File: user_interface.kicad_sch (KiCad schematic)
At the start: 26 parts, among them J10 Line out, J11 Headphone, J2 SWD, J3 I2C, J4 GPIO_A, J5 GPIO_B, J6 SPI, J9 Serial

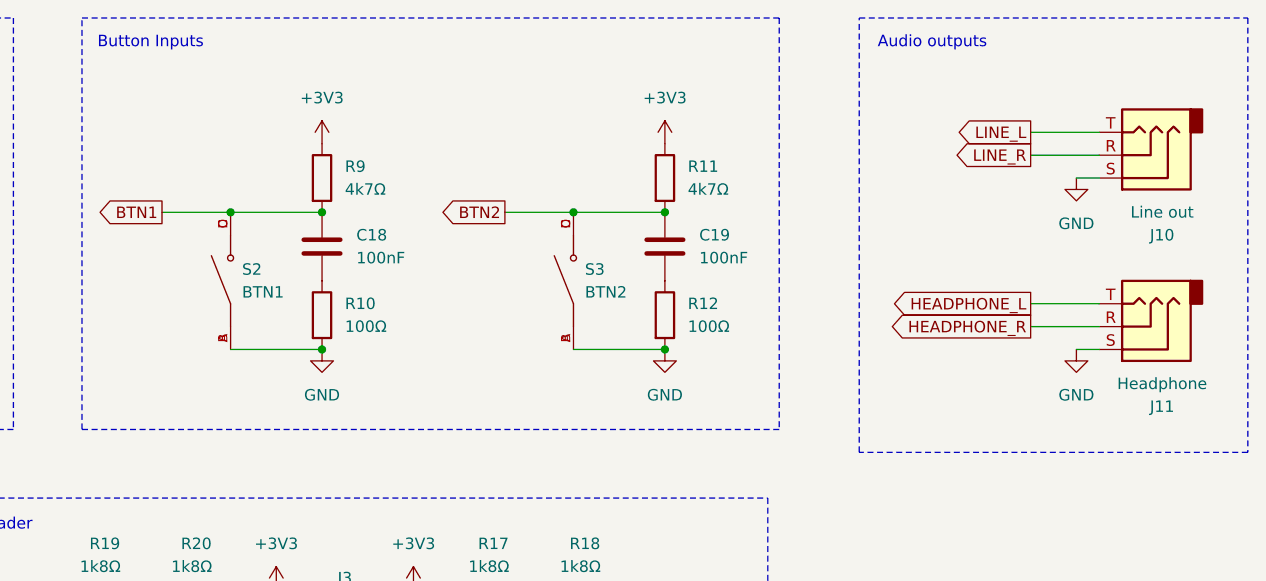
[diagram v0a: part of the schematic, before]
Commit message: Updated schematic with parts found in JLCPCB parts database. Updated footprints, 3d models for those items. All schematic symbols now have LCSC part numbers, footprints and 3D models. No PCB layout has been done.
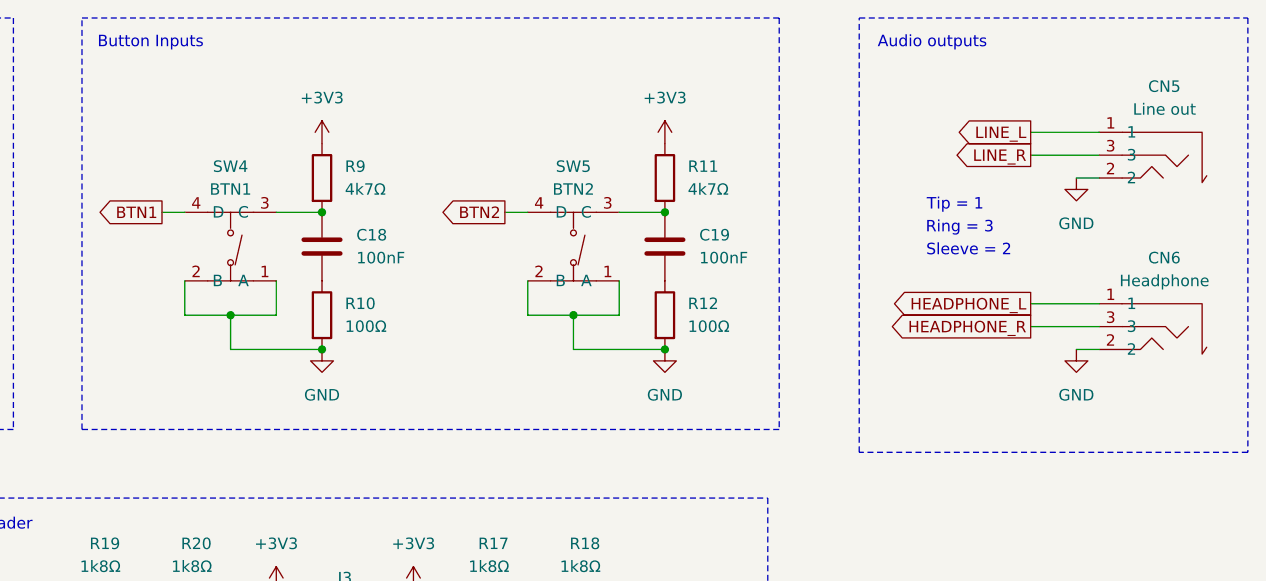
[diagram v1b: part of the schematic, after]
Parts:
- removed J10: Line out, symbol Connector_Audio:AudioJack3
- removed J11: Headphone, symbol Connector_Audio:AudioJack3
- removed S2: BTN1, stm-midi-poc1:SW_TS-1187A-B-A-B, symbol TS-1187A-B-A-B:TS-1187A-B-A-B
- removed S3: BTN2, stm-midi-poc1:SW_TS-1187A-B-A-B, symbol TS-1187A-B-A-B:TS-1187A-B-A-B
- added CN5: Line out, easyeda2kicad:AUDIO-SMD_PJ-321A-4A, symbol easyeda2kicad:PJ-321A-4A
- added CN6: Headphone, easyeda2kicad:AUDIO-SMD_PJ-321A-4A, symbol easyeda2kicad:PJ-321A-4A
- added SW4: BTN1, easyeda2kicad:SW-SMD_4P-L5.1-W5.1-P3.70-LS6.5-TL-2, symbol easyeda2kicad:TS-1187A-B-A-B
- added SW5: BTN2, easyeda2kicad:SW-SMD_4P-L5.1-W5.1-P3.70-LS6.5-TL-2, symbol easyeda2kicad:TS-1187A-B-A-B
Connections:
- net BTN1: now also SW4.4 (D); no longer C18.1, R9.2
- net BTN2: now also SW5.4 (D); no longer C19.1, R11.2
- net GND: now also CN5.2, CN6.2, SW4.1 (A), SW4.2 (B), SW5.1 (A), SW5.2 (B)
- net HEADPHONE_L: now also CN6.1
- net HEADPHONE_R: now also CN6.3
- net LINE_L: now also CN5.1
- net LINE_R: now also CN5.3
- new net: C18.1, R9.2, SW4.3 (C)
- new net: C19.1, R11.2, SW5.3 (C)
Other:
- note added: "Ring = 3"
- note added: "Sleeve = 2"
- note added: "Tip = 1"

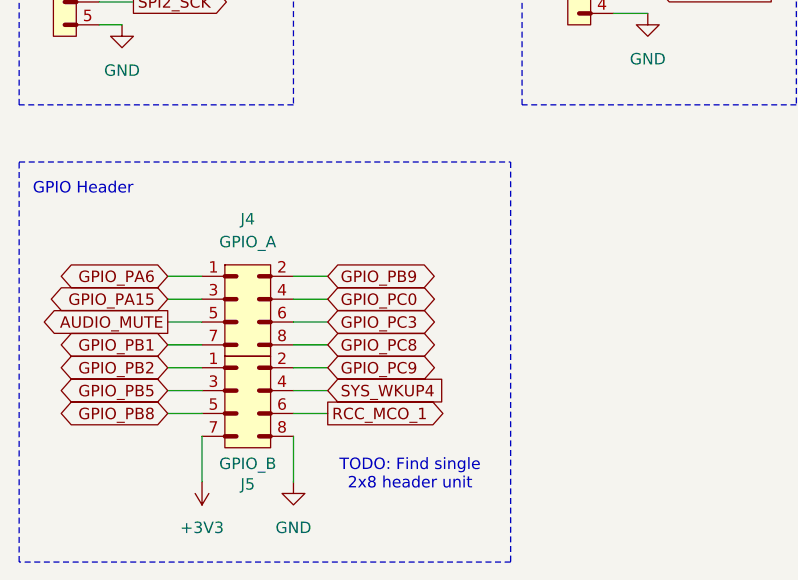
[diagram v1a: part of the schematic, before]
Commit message: Group PCB components together more. Replace 2x2x4 by 1x2x8 connector.
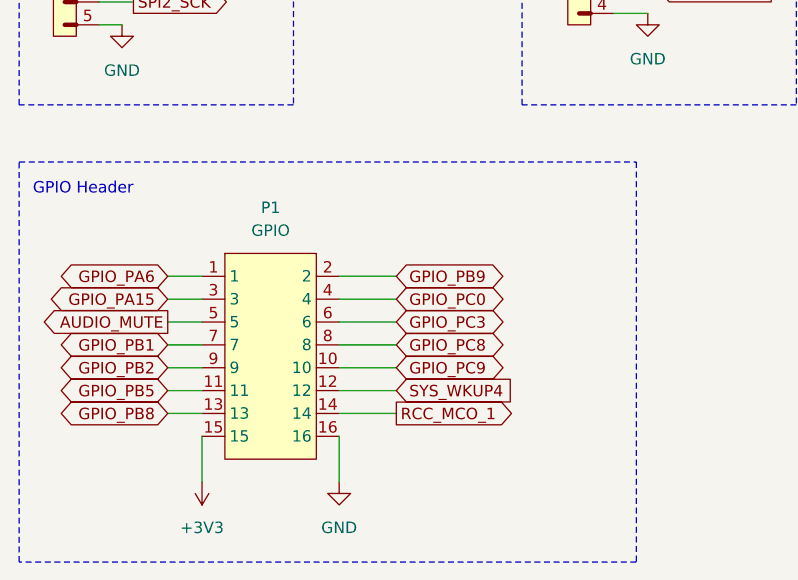
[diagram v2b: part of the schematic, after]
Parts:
- removed J4: GPIO_A, Connector_PinHeader_2.54mm:PinHeader_2x04_P2.54mm_Vertical, symbol PCM_SL_Pin_Headers:PINHD_2x4_Male
- removed J5: GPIO_B, Connector_PinHeader_2.54mm:PinHeader_2x04_P2.54mm_Vertical, symbol PCM_SL_Pin_Headers:PINHD_2x4_Male
- added P1: GPIO, easyeda2kicad:HDR-TH_16P-P2.54-V-M-R2-C8-S2.54, symbol easyeda2kicad:Header-Male-2.54_2x8
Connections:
- net +3V3: now also P1.15
- net AUDIO_MUTE: now also P1.5
- net GND: now also P1.16
- net GPIO_PA15: now also P1.3
- net GPIO_PA6: now also P1.1
- net GPIO_PB1: now also P1.7
- net GPIO_PB2: now also P1.9
- net GPIO_PB5: now also P1.11
- net GPIO_PB8: now also P1.13
- net GPIO_PB9: now also P1.2
- net GPIO_PC0: now also P1.4
- net GPIO_PC3: now also P1.6
- net GPIO_PC8: now also P1.8
- net GPIO_PC9: now also P1.10
- net RCC_MCO_1: now also P1.14
- net SYS_WKUP4: now also P1.12
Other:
- note removed: "TODO: Find single 2x8 header unit"

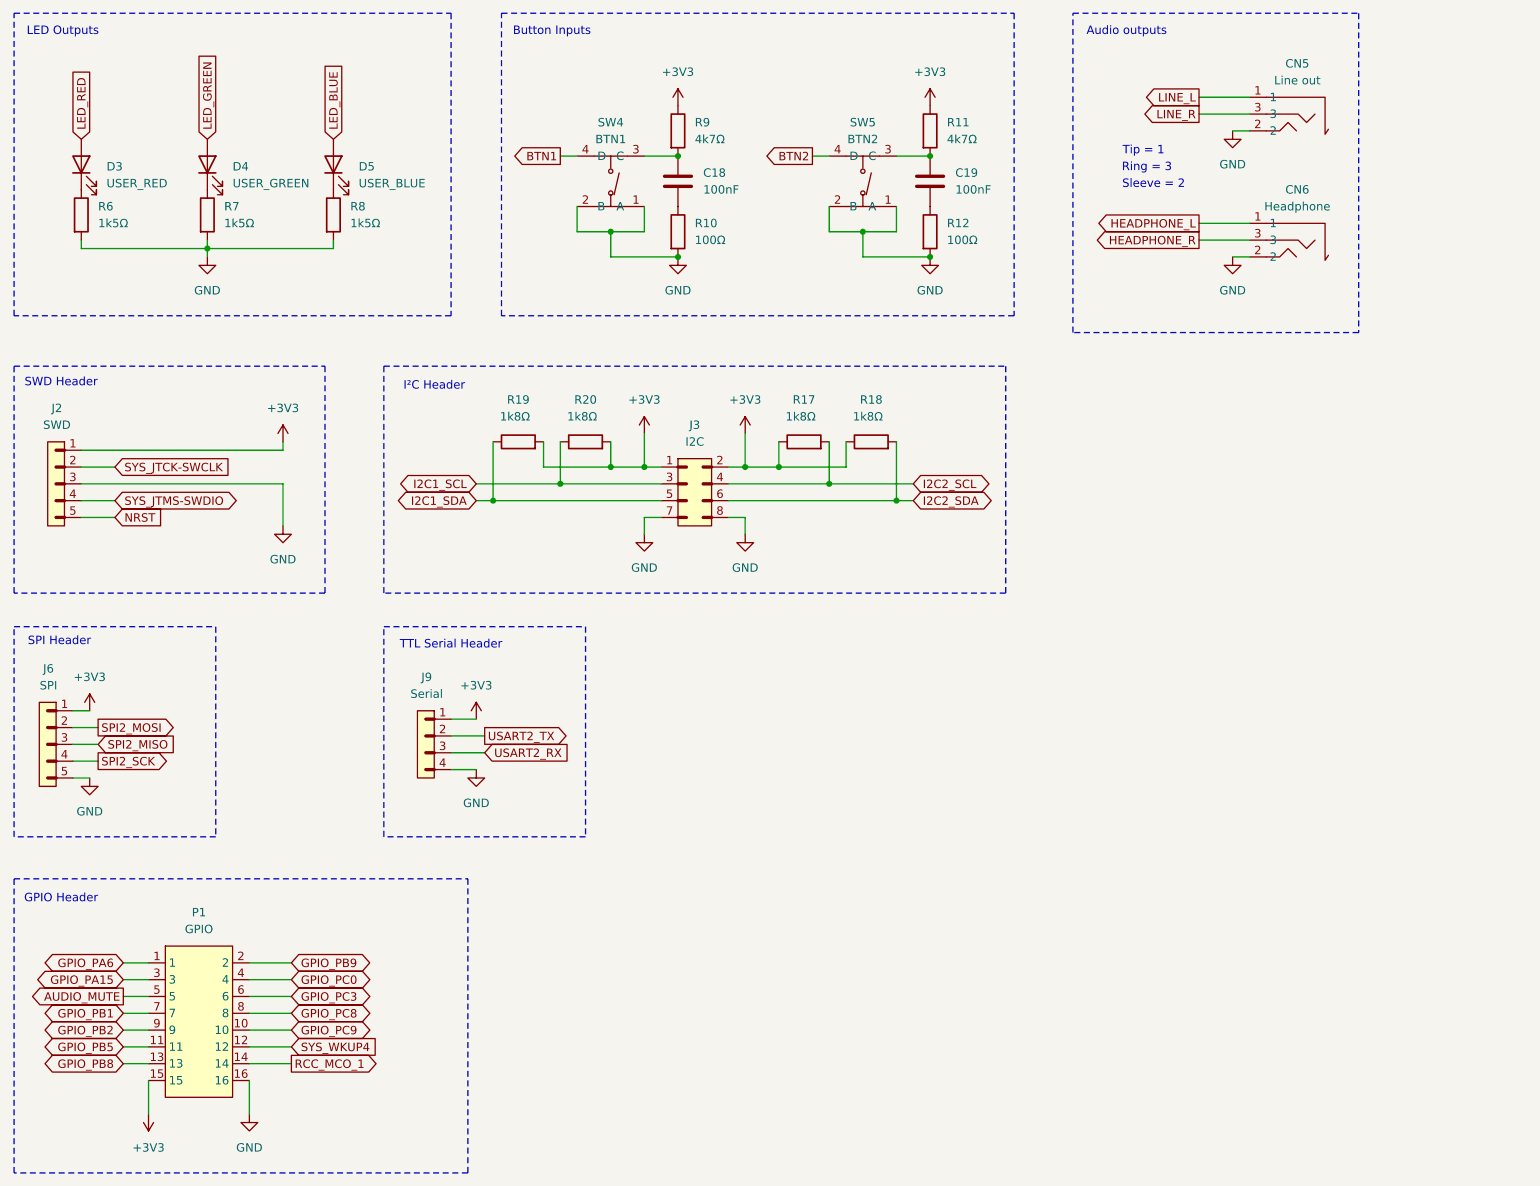
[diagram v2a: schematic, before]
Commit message: Create PCB outline and move components into better locations. (Not done yet!) Update schematic a little bit with additional nets and clarifications. Add mounting holes. Unify components/footprints.
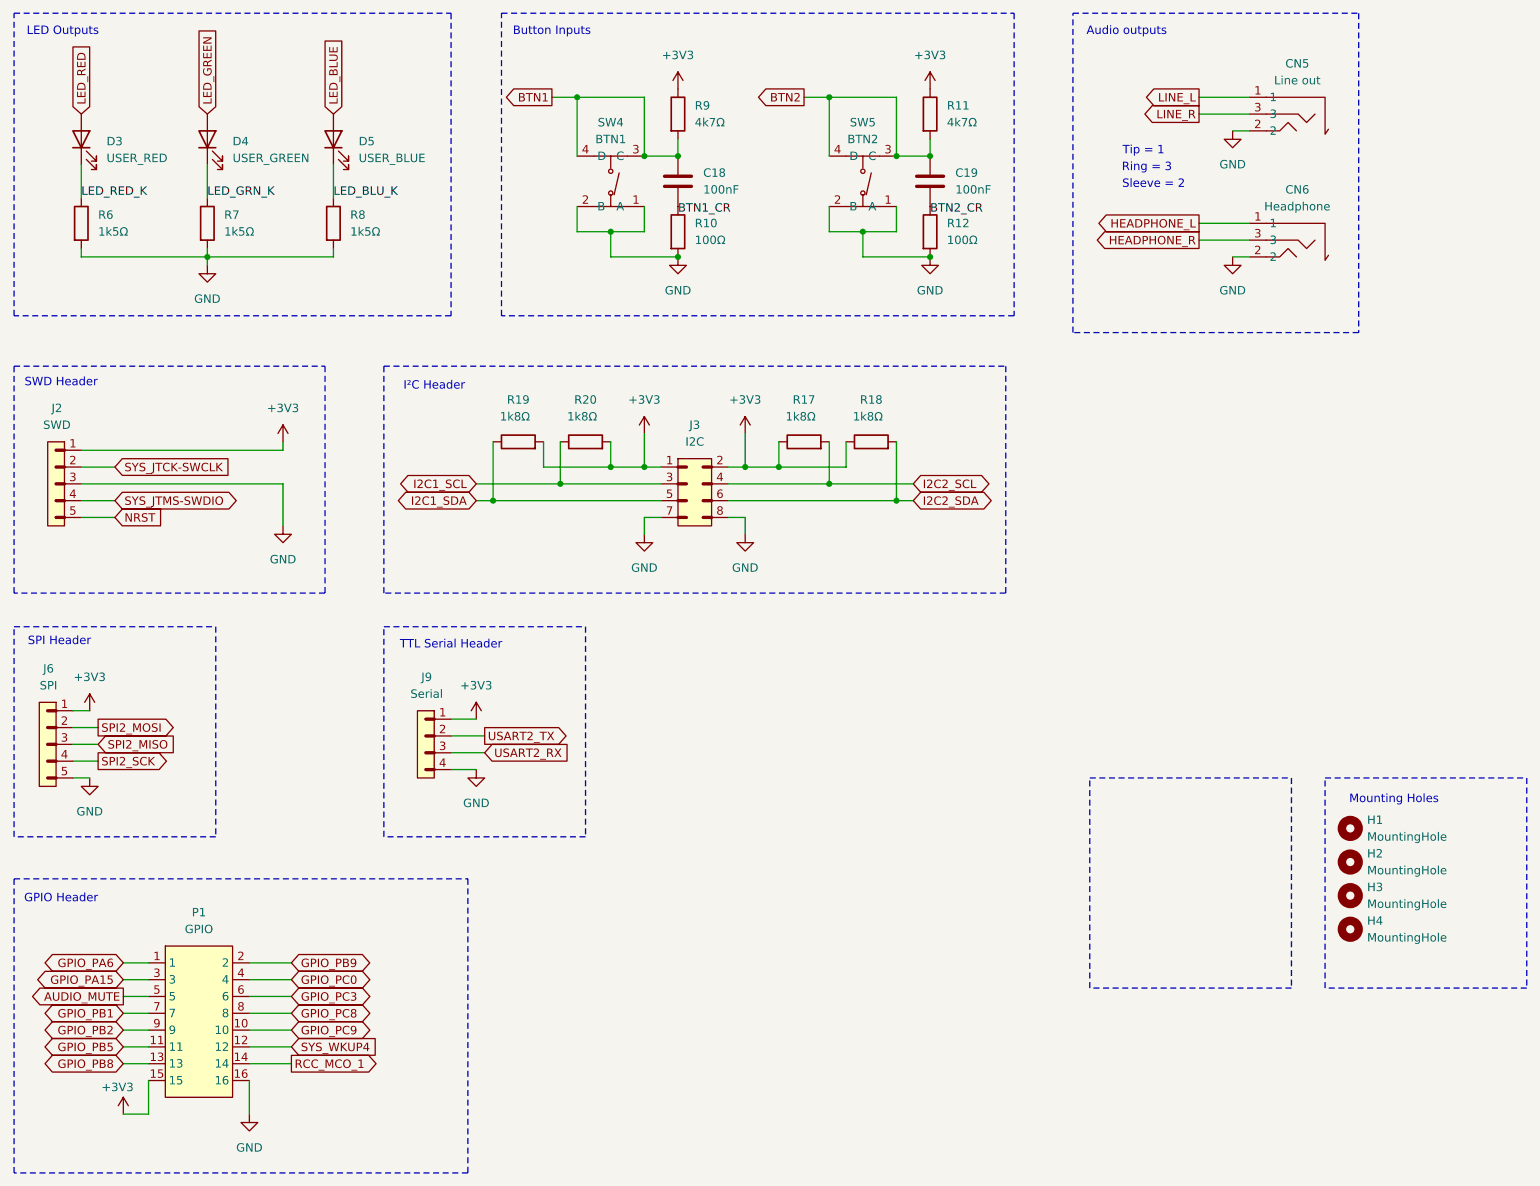
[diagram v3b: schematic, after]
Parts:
- added H1, H2, H3, H4: MountingHole, MountingHole:MountingHole_2.2mm_M2, symbol Mechanical:MountingHole
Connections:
- net BTN1: now also C18.1, R9.2, SW4.3 (C)
- net BTN2: now also C19.1, R11.2, SW5.3 (C)
- net LED_BLU_K: now reaches D5.1 (K), R8.1
- net LED_RED_K: now reaches D3.1 (K), R6.1
- net LED_GRN_K: now reaches D4.1 (K), R7.1
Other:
- note added: "Mounting Holes"
- moved on the sheet: D3, D4, D5, R11, R6, R7, R8, R9

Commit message: Work on power section and some miscellaneous small areas
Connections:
- net BTN1_CR: now also C18.2, R10.1
- net BTN2_CR: now also C19.2, R12.1
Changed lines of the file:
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@@
 	)
 	(label "BTN1_CR"
-		(at 133.35 49.53 0)
+		(at 133.35 48.26 0)
 		(fields_autoplaced yes)
 		(effects
@@
 	)
 	(label "BTN2_CR"
-		(at 171.45 49.53 0)
+		(at 171.45 48.26 0)
 		(fields_autoplaced yes)
 		(effects

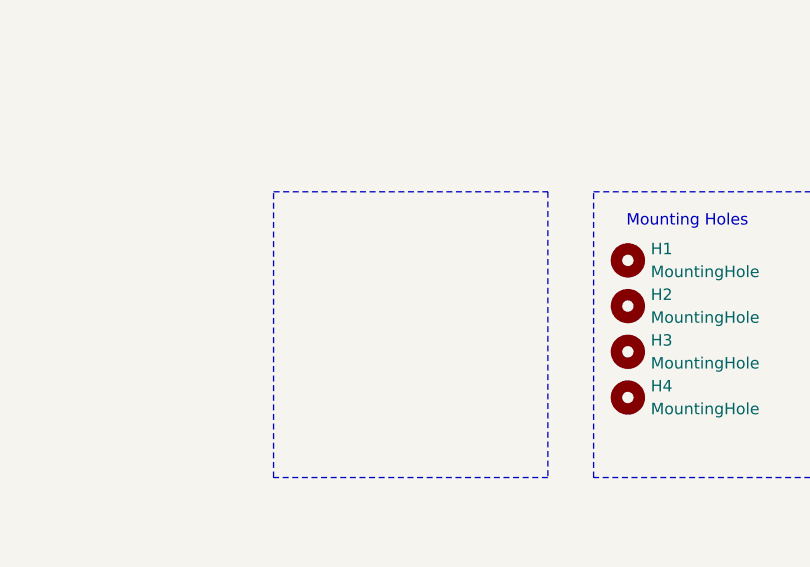
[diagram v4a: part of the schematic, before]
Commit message: Modify power to analog side.
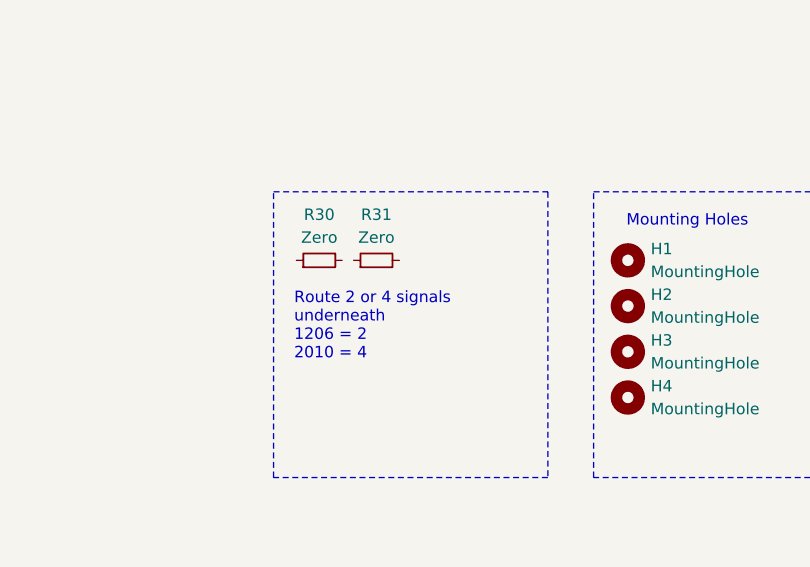
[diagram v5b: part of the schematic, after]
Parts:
- added R30: Zero, Resistor_SMD:R_2010_5025Metric, symbol Device:R_Small
- added R31: Zero, Resistor_SMD:R_1206_3216Metric, symbol Device:R_Small
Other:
- note added: "Route 2 or 4 signals underneath 1206 = 2 2010 = 4"
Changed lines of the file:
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@@
 		)
 	)
+	(text "Route 2 or 4 signals\nunderneath\n1206 = 2\n2010 = 4"
+		(exclude_from_sim no)
+		(at 197.866 145.796 0)
+		(effects
+			(font
+				(size 1.27 1.27)
+			)
+			(justify left top)
+		)
+	)
 	(text "Audio outputs"
 		(exclude_from_sim no)
@@
 	)
 	(symbol
+		(lib_id "Device:R_Small")
+		(at 207.01 142.24 90)
+		(unit 1)
+		(exclude_from_sim no)
+		(in_bom yes)
+		(on_board yes)
+		(dnp no)
+		(property "Reference" "R31"
+			(at 207.01 137.16 90)
+			(effects
+				(font
+					(size 1.27 1.27)
+				)
+			)
+		)
+		(property "Value" "Zero"
+			(at 207.01 139.7 90)
+			(effects
+				(font
+					(size 1.27 1.27)
+				)
+			)
+		)
+		(property "Footprint" "Resistor_SMD:R_1206_3216Metric"
+			(at 207.01 142.24 0)
+			(effects
+				(font
+					(size 1.27 1.27)
+				)
+				(hide yes)
+			)
+		)
+		(property "Datasheet" "~"
+			(at 207.01 142.24 0)
+			(effects
+				(font
+					(size 1.27 1.27)
+				)
+				(hide yes)
+			)
+		)
+		(property "Description" "Resistor, small symbol"
+			(at 207.01 142.24 0)
+			(effects
+				(font
+					(size 1.27 1.27)
+				)
+				(hide yes)
+			)
+		)
+		(property "LCSC" ""
+			(at 207.01 142.24 0)
+			(effects
+				(font
+					(size 1.27 1.27)
+				)
+				(hide yes)
+			)
+		)
+		(property "DPFNOTES" "For Routing"
+			(at 207.01 142.24 0)
+			(effects
+				(font
+					(size 1.27 1.27)
+				)
+				(hide yes)
+			)
+		)
+		(property "DPFURL" ""
+			(at 207.01 142.24 0)
+			(effects
+				(font
+					(size 1.27 1.27)
+				)
+				(hide yes)
+			)
+		)
+		(pin "1"
+		)
+		(pin "2"
+		)
+		(instances
+			(project "stm-midi-poc1"
+				(path "/7cd74113-1f92-4dcc-8610-19aa9fc81e5f/96c396b4-5394-4a50-9288-ad4476d1492f"
+					(reference "R31")
+					(unit 1)
+				)
+			)
+		)
+	)
+	(symbol
 		(lib_id "power:+3V3")
 		(at 49.53 185.42 0)
@@
 					(unit 1)
 				)
+			)
+		)
+	)
+	(symbol
+		(lib_id "Device:R_Small")
+		(at 200.66 142.24 90)
+		(unit 1)
+		(exclude_from_sim no)
+		(in_bom yes)
+		(on_board yes)
+		(dnp no)
+		(fields_autoplaced yes)
+		(property "Reference" "R30"
+			(at 200.66 137.16 90)
+			(effects
+				(font
+					(size 1.27 1.27)
+				)
+			)
+		)
+		(property "Value" "Zero"
+			(at 200.66 139.7 90)
+			(effects
+				(font
+					(size 1.27 1.27)
+				)
+			)
+		)
+		(property "Footprint" "Resistor_SMD:R_2010_5025Metric"
+			(at 200.66 142.24 0)
+			(effects
+				(font
+					(size 1.27 1.27)
+				)
+				(hide yes)
+			)
+		)
+		(property "Datasheet" "~"
+			(at 200.66 142.24 0)
+			(effects
+				(font
+					(size 1.27 1.27)
+				)
+				(hide yes)
+			)
+		)
+		(property "Description" "Resistor, small symbol"
+			(at 200.66 142.24 0)
+			(effects
+				(font
+					(size 1.27 1.27)
+				)
+				(hide yes)
+			)
+		)
+		(property "LCSC" ""
+			(at 200.66 142.24 0)
+			(effects
+				(font
+					(size 1.27 1.27)
+				)
+				(hide yes)
+			)
+		)
+		(property "DPFNOTES" "For Routing"
+			(at 200.66 142.24 0)
+			(effects
+				(font
+					(size 1.27 1.27)
+				)
+				(hide yes)
+			)
+		)
+		(property "DPFURL" ""
+			(at 200.66 142.24 0)
+			(effects
+				(font
+					(size 1.27 1.27)
+				)
+				(hide yes)
+			)
+		)
+		(pin "1"
+		)
+		(pin "2"
+		)
+		(instances
+			(project "stm-midi-poc1"
+				(path "/7cd74113-1f92-4dcc-8610-19aa9fc81e5f/96c396b4-5394-4a50-9288-ad4476d1492f"
+					(reference "R30")
+					(unit 1)
+				)
